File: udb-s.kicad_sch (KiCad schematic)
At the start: 10 parts, among them J1 TYPE-C-31-M-12, J2 78171-0004

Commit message: made production files + BOM
generated the production files and filled out the BOM using lcsc components
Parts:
- D1: footprint Diode_SMD:D_SOD-123F -> Diode_SMD:D_SOD-123; LCSC Part Number C502546 -> C85649; Package SOD-523 -> SOD-123F
- D2: LCSC Part Number (none) -> C78442
- FB1: LCSC Part Number C1017 -> C21286
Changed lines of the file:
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@@
 			)
 		)
-		(property "LCSC Part Number" "C1017"
+		(property "LCSC Part Number" "C21286"
 			(at 122.555 103.505 0)
 			(effects
@@
 			)
 		)
+		(property "Manufacturer" ""
+			(at 176.53 102.87 0)
+			(effects
+				(font
+					(size 1.27 1.27)
+				)
+				(hide yes)
+			)
+		)
+		(property "Manufacturer Part Number" ""
+			(at 176.53 102.87 0)
+			(effects
+				(font
+					(size 1.27 1.27)
+				)
+				(hide yes)
+			)
+		)
+		(property "LCSC Part Number" "C78442"
+			(at 176.53 102.87 0)
+			(effects
+				(font
+					(size 1.27 1.27)
+				)
+				(hide yes)
+			)
+		)
+		(property "Package" ""
+			(at 176.53 102.87 0)
+			(effects
+				(font
+					(size 1.27 1.27)
+				)
+				(hide yes)
+			)
+		)
 		(pin "1"
 		)
@@
 			)
 		)
-		(property "Footprint" "Diode_SMD:D_SOD-123F"
+		(property "Footprint" "Diode_SMD:D_SOD-123"
 			(at 223.52 50.8 0)
 			(effects
@@
 			)
 		)
-		(property "LCSC Part Number" "C502546"
+		(property "LCSC Part Number" "C85649"
 			(at 228.6 50.8 0)
 			(effects
@@
 			)
 		)
-		(property "Package" "SOD-523"
+		(property "Package" "SOD-123F"
 			(at 228.6 50.8 0)
 			(effects

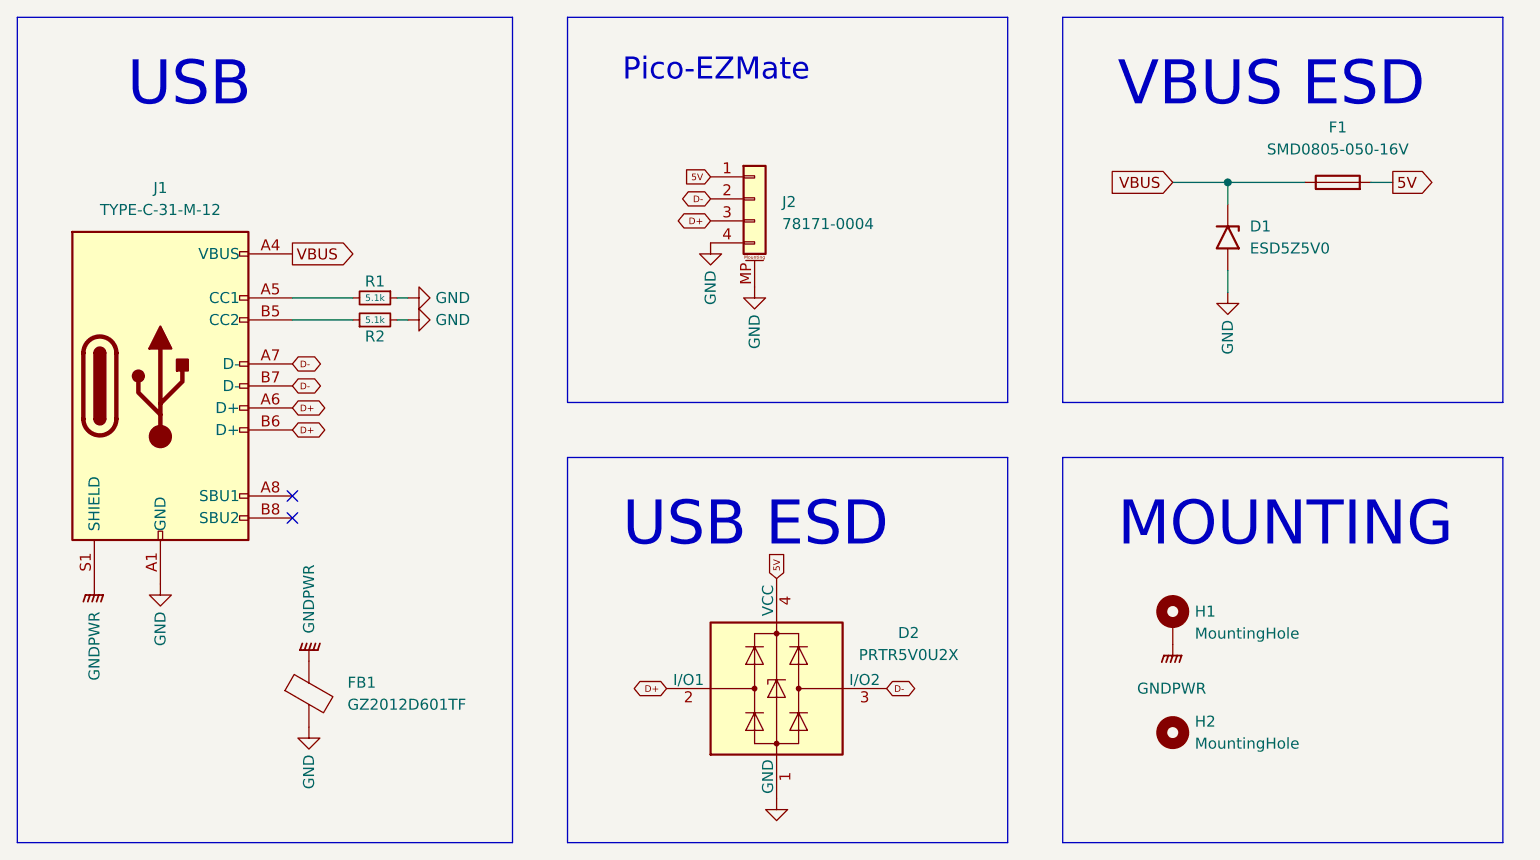
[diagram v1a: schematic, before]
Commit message: swapped to SRV05-4
swapped the esd chip to the SRV05-4 and removed the singular diode because its built into the esd chip
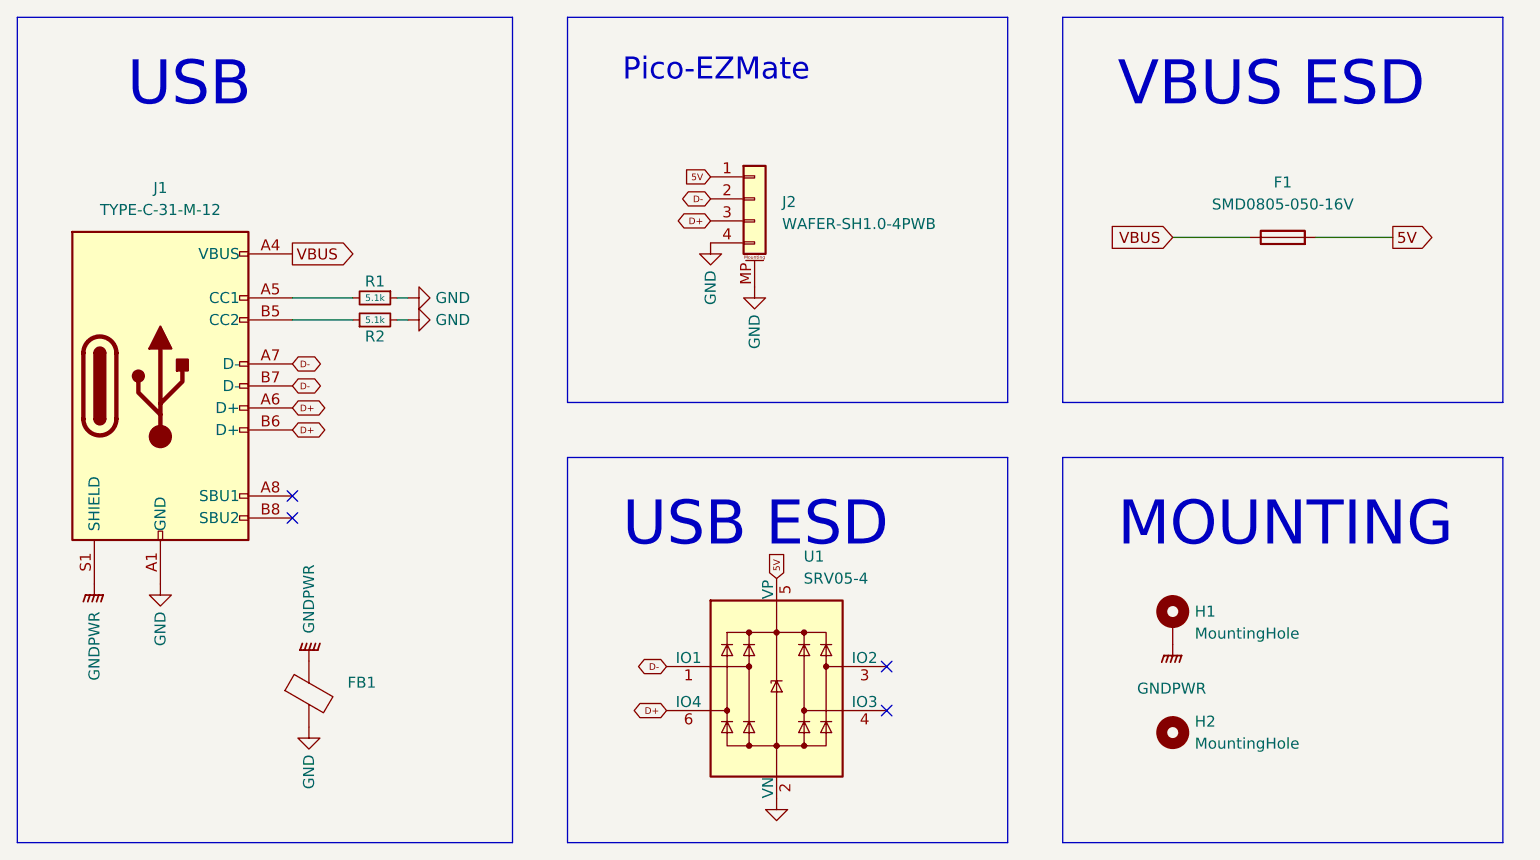
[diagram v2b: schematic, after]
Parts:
- removed D1: ESD5Z5V0, Diode_SMD:D_SOD-123, symbol Diode:SMF6V0A
- removed D2: PRTR5V0U2X, Package_TO_SOT_SMD:SOT-143, symbol Power_Protection:PRTR5V0U2X
- added U1: SRV05-4, PCM_marbastlib-various:SOT-23-6-routable, symbol PCM_marbastlib-various:SRV05-4
- F1: footprint Fuse:Fuse_1206_3216Metric -> Fuse:Fuse_0805_2012Metric
- FB1: value GZ2012D601TF -> ~; Manufacturer Sunlord -> (none); Manufacturer Part Number GZ2012D601TF -> (none)
- J2: value 78171-0004 -> WAFER-SH1.0-4PWB; LCSC Part Number C588524 -> C3029343; Manufacturer MOLEX -> (none); Manufacturer Part Number 78171-0004 -> (none)
- R1, R2: LCSC Part Number (none) -> C27834
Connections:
- net 5V: now also U1.5 (VP)
- net D+: now also U1.6 (IO4)
- net D-: now also U1.1 (IO1)
- net GND: now also U1.2 (VN)
- no-connect marks 2 -> 4
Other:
- moved on the sheet: F1
